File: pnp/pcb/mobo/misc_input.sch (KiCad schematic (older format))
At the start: 9 parts, among them J18 R_LIMIT, J19 P_LIMIT, J20 C_LIMIT, J60 X_LIMIT, J61 Y_LIMIT, J62 Z_LIMIT, J65 ADC_AUX_1, J66 ADC_AUX_2, U6 ‎MPXV5100GC6U

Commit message: took a crack at starting vacuum sensor schematic
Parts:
- removed U6: ‎MPXV5100GC6U, index:‎MPXV5100GC6U, symbol mobo-rescue:‎MPXV5100GC6U-index
- added R? (x8): 10K, symbol Device:R_Small
- added R?: 25K Precision, symbol Device:R_Small
- added U? (x2): 2SMPP-03, symbol index:2SMPP-03
- added U?: INA128, symbol Amplifier_Instrumentation:INA128
- added U? (x6): LM358, symbol Amplifier_Operational:LM358
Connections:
- net labels added: VAC2_SIG
- wire segments 34 -> 75
- no-connect marks 5 -> 4

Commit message: tentative schematic for vacuum, without the right symbol for in-amps
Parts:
- removed U?: 2SMPP-03, symbol index:2SMPP-03
- removed U? (x3): LM358, symbol Amplifier_Operational:LM358
- added R? (x8): 10K, symbol Device:R_Small
- added R?: 25K Precision, symbol Device:R_Small
- added U?: 2SMPP-03, symbol index:2SMPP-03
- added U?: INA128, symbol Amplifier_Instrumentation:INA128
- added U? (x3): LM358, symbol Amplifier_Operational:LM358
- gave numbers to parts that had none: 12
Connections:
- net labels added: +12V
- wire segments 75 -> 118
- no-connect marks 4 -> 6
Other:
- note added: "make this in-amp actually one IC"

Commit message: added reverse polarity protection with a p channel fet
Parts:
- R22, R?: value 10K -> 1K
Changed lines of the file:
@@
 P 6150 2150
 F 0 "R22" H 6000 2200 50  0000 L CNN
-F 1 "10K" H 5800 2100 50  0000 L CNN
+F 1 "1K" H 5800 2100 50  0000 L CNN
 F 2 "" H 6150 2150 50  0001 C CNN
 F 3 "~" H 6150 2150 50  0001 C CNN
@@
 P 6150 4900
 F 0 "R?" H 6000 4950 50  0000 L CNN
-F 1 "10K" H 5800 4850 50  0000 L CNN
+F 1 "1K" H 5800 4850 50  0000 L CNN
 F 2 "" H 6150 4900 50  0001 C CNN
 F 3 "~" H 6150 4900 50  0001 C CNN

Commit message: assigned a footprint to the instrumentation amplifier, deleted all traces from old layout
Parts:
- R19, R20, R21, R22, R23, R24, R25, R26, R27: footprint (none) -> Resistor_SMD:R_0805_2012Metric_Pad1.15x1.40mm_HandSolder
- R28, R29, R30, R31, R32, R33, R34, R35, R36: renamed from R?; footprint (none) -> Resistor_SMD:R_0805_2012Metric_Pad1.15x1.40mm_HandSolder
- U10: footprint (none) -> Package_SO:SOIC-16_3.9x9.9mm_P1.27mm
- gave numbers to parts that had none: 5
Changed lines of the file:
@@
 VAC2_SIG
 $Comp
-L index:2SMPP-03 U?
+L index:2SMPP-03 U12
 U 1 1 5F80C429
 P 4650 2600
-F 0 "U?" H 4650 2577 50  0000 C CNN
+F 0 "U12" H 4650 2577 50  0000 C CNN
 F 1 "2SMPP-03" H 4650 2486 50  0000 C CNN
 F 2 "" H 4650 2600 50  0001 C CNN
@@
 F 0 "U10" H 6600 2300 50  0000 L CNN
 F 1 "INA128" H 6700 2050 50  0000 L CNN
-F 2 "" H 6600 2150 50  0001 C CNN
+F 2 "Package_SO:SOIC-16_3.9x9.9mm_P1.27mm" H 6600 2150 50  0001 C CNN
 F 3 "http://www.ti.com/lit/ds/symlink/ina128.pdf" H 6600 2150 50  0001 C CNN
 	1    6500 2150
@@
 F 0 "R22" H 6000 2200 50  0000 L CNN
 F 1 "1K" H 5800 2100 50  0000 L CNN
-F 2 "" H 6150 2150 50  0001 C CNN
+F 2 "Resistor_SMD:R_0805_2012Metric_Pad1.15x1.40mm_HandSolder" H 6150 2150 50  0001 C CNN
 F 3 "~" H 6150 2150 50  0001 C CNN
 	1    6150 2150
@@
 F 0 "R19" H 3000 1600 50  0000 L CNN
 F 1 "10K" H 2950 1500 50  0000 L CNN
-F 2 "" H 3150 1550 50  0001 C CNN
+F 2 "Resistor_SMD:R_0805_2012Metric_Pad1.15x1.40mm_HandSolder" H 3150 1550 50  0001 C CNN
 F 3 "~" H 3150 1550 50  0001 C CNN
 	1    3150 1550
@@
 F 0 "R20" H 3000 2000 50  0000 L CNN
 F 1 "10K" H 2950 1900 50  0000 L CNN
-F 2 "" H 3150 1950 50  0001 C CNN
+F 2 "Resistor_SMD:R_0805_2012Metric_Pad1.15x1.40mm_HandSolder" H 3150 1950 50  0001 C CNN
 F 3 "~" H 3150 1950 50  0001 C CNN
 	1    3150 1950
@@
 F 0 "R21" V 4000 2450 50  0000 L CNN
 F 1 "25K Precision" V 3800 2050 50  0000 L CNN
-F 2 "" H 3900 2500 50  0001 C CNN
+F 2 "Resistor_SMD:R_0805_2012Metric_Pad1.15x1.40mm_HandSolder" H 3900 2500 50  0001 C CNN
 F 3 "~" H 3900 2500 50  0001 C CNN
 	1    3900 2500
@@
 F 0 "R24" H 7450 1900 50  0000 L CNN
 F 1 "10K" H 7400 1800 50  0000 L CNN
-F 2 "" H 7600 1850 50  0001 C CNN
+F 2 "Resistor_SMD:R_0805_2012Metric_Pad1.15x1.40mm_HandSolder" H 7600 1850 50  0001 C CNN
 F 3 "~" H 7600 1850 50  0001 C CNN
 	1    7600 1850
@@
 F 0 "R25" H 7450 2450 50  0000 L CNN
 F 1 "10K" H 7400 2350 50  0000 L CNN
-F 2 "" H 7600 2400 50  0001 C CNN
+F 2 "Resistor_SMD:R_0805_2012Metric_Pad1.15x1.40mm_HandSolder" H 7600 2400 50  0001 C CNN
 F 3 "~" H 7600 2400 50  0001 C CNN
 	1    7600 2400
@@
 F 0 "R26" H 7800 2450 50  0000 L CNN
 F 1 "10K" H 7750 2350 50  0000 L CNN
-F 2 "" H 7950 2400 50  0001 C CNN
+F 2 "Resistor_SMD:R_0805_2012Metric_Pad1.15x1.40mm_HandSolder" H 7950 2400 50  0001 C CNN
 F 3 "~" H 7950 2400 50  0001 C CNN
 	1    7950 2400
@@
 F 0 "R23" V 7250 2200 50  0000 L CNN
 F 1 "10K" V 7250 2000 50  0000 L CNN
-F 2 "" H 7350 2150 50  0001 C CNN
+F 2 "Resistor_SMD:R_0805_2012Metric_Pad1.15x1.40mm_HandSolder" H 7350 2150 50  0001 C CNN
 F 3 "~" H 7350 2150 50  0001 C CNN
 	1    7350 2150
@@
 F 0 "R27" V 7900 1600 50  0000 L CNN
 F 1 "10K" V 7900 1400 50  0000 L CNN
-F 2 "" H 8000 1550 50  0001 C CNN
+F 2 "Resistor_SMD:R_0805_2012Metric_Pad1.15x1.40mm_HandSolder" H 8000 1550 50  0001 C CNN
 F 3 "~" H 8000 1550 50  0001 C CNN
 	1    8000 1550
@@
 make this in-amp actually one IC
 $Comp
-L index:2SMPP-03 U?
+L index:2SMPP-03 U13
 U 1 1 5F829496
 P 4650 5350
-F 0 "U?" H 4650 5327 50  0000 C CNN
+F 0 "U13" H 4650 5327 50  0000 C CNN
 F 1 "2SMPP-03" H 4650 5236 50  0000 C CNN
 F 2 "" H 4650 5350 50  0001 C CNN
@@
 $EndComp
 $Comp
-L Amplifier_Instrumentation:INA128 U?
+L Amplifier_Instrumentation:INA128 U14
 U 1 1 5F82949C
 P 6500 4900
-F 0 "U?" H 6600 5050 50  0000 L CNN
+F 0 "U14" H 6600 5050 50  0000 L CNN
 F 1 "INA128" H 6700 4800 50  0000 L CNN
 F 2 "" H 6600 4900 50  0001 C CNN
@@
 $EndComp
 $Comp
-L Device:R_Small R?
+L Device:R_Small R31
 U 1 1 5F8294A2
 P 6150 4900
-F 0 "R?" H 6000 4950 50  0000 L CNN
+F 0 "R31" H 6000 4950 50  0000 L CNN
 F 1 "1K" H 5800 4850 50  0000 L CNN
-F 2 "" H 6150 4900 50  0001 C CNN
+F 2 "Resistor_SMD:R_0805_2012Metric_Pad1.15x1.40mm_HandSolder" H 6150 4900 50  0001 C CNN
 F 3 "~" H 6150 4900 50  0001 C CNN
 	1    6150 4900
@@
 	6150 5000 6200 5000
 $Comp
-L power:GND #PWR?
+L power:GND #PWR0190
 U 1 1 5F8294AA
 P 6500 5300
-F 0 "#PWR?" H 6500 5050 50  0001 C CNN
+F 0 "#PWR0190" H 6500 5050 50  0001 C CNN
 F 1 "GND" H 6600 5200 50  0000 C CNN
 F 2 "" H 6500 5300 50  0001 C CNN
@@
 	6500 4600 6500 4500
 $Comp
-L Amplifier_Operational:LM358 U?
+L Amplifier_Operational:LM358 U11
 U 1 1 5F8294B7
 P 3800 4600
-F 0 "U?" H 3800 4967 50  0000 C CNN
+F 0 "U11" H 3800 4967 50  0000 C CNN
 F 1 "LM358" H 3800 4876 50  0000 C CNN
 F 2 "" H 3800 4600 50  0001 C CNN
@@
 $EndComp
 $Comp
-L Amplifier_Operational:LM358 U?
+L Amplifier_Operational:LM358 U6
 U 2 1 5F8294BD
 P 8250 4800
-F 0 "U?" H 8250 5167 50  0000 C CNN
+F 0 "U6" H 8250 5167 50  0000 C CNN
 F 1 "LM358" H 8250 5076 50  0000 C CNN
 F 2 "" H 8250 4800 50  0001 C CNN
@@
 $EndComp
 $Comp
-L Amplifier_Operational:LM358 U?
+L Amplifier_Operational:LM358 U11
 U 3 1 5F8294C3
 P 5750 4050
-F 0 "U?" H 5708 4096 50  0000 L CNN
+F 0 "U11" H 5708 4096 50  0000 L CNN
 F 1 "LM358" H 5708 4005 50  0000 L CNN
 F 2 "" H 5750 4050 50  0001 C CNN
@@
 $EndComp
 $Comp
-L Device:R_Small R?
+L Device:R_Small R28
 U 1 1 5F8294C9
 P 3150 4300
-F 0 "R?" H 3000 4350 50  0000 L CNN
+F 0 "R28" H 3000 4350 50  0000 L CNN
 F 1 "10K" H 2950 4250 50  0000 L CNN
-F 2 "" H 3150 4300 50  0001 C CNN
+F 2 "Resistor_SMD:R_0805_2012Metric_Pad1.15x1.40mm_HandSolder" H 3150 4300 50  0001 C CNN
 F 3 "~" H 3150 4300 50  0001 C CNN
 	1    3150 4300
@@
 $EndComp
 $Comp
-L Device:R_Small R?
+L Device:R_Small R29
 U 1 1 5F8294CF
 P 3150 4700
-F 0 "R?" H 3000 4750 50  0000 L CNN
+F 0 "R29" H 3000 4750 50  0000 L CNN
 F 1 "10K" H 2950 4650 50  0000 L CNN
-F 2 "" H 3150 4700 50  0001 C CNN
+F 2 "Resistor_SMD:R_0805_2012Metric_Pad1.15x1.40mm_HandSolder" H 3150 4700 50  0001 C CNN
 F 3 "~" H 3150 4700 50  0001 C CNN
 	1    3150 4700
@@
 $EndComp
 $Comp
-L power:+5V #PWR?
+L power:+5V #PWR0214
 U 1 1 5F8294D5
 P 3500 3950
-F 0 "#PWR?" H 3500 3800 50  0001 C CNN
+F 0 "#PWR0214" H 3500 3800 50  0001 C CNN
 F 1 "+5V" H 3515 4123 50  0000 C CNN
 F 2 "" H 3500 3950 50  0001 C CNN
@@
 	3150 3950 3500 3950
 $Comp
-L power:GND #PWR?
+L power:GND #PWR0215
 U 1 1 5F8294E1
 P 3500 5250
-F 0 "#PWR?" H 3500 5000 50  0001 C CNN
+F 0 "#PWR0215" H 3500 5000 50  0001 C CNN
 F 1 "GND" H 3600 5150 50  0000 C CNN
 F 2 "" H 3500 5250 50  0001 C CNN
@@
 	5200 4950 5100 4950
 $Comp
-L Device:R_Small R?
+L Device:R_Small R30
 U 1 1 5F8294EC
 P 3900 5250
-F 0 "R?" V 4000 5200 50  0000 L CNN
+F 0 "R30" V 4000 5200 50  0000 L CNN
 F 1 "25K Precision" V 3800 4800 50  0000 L CNN
-F 2 "" H 3900 5250 50  0001 C CNN
+F 2 "Resistor_SMD:R_0805_2012Metric_Pad1.15x1.40mm_HandSolder" H 3900 5250 50  0001 C CNN
 F 3 "~" H 3900 5250 50  0001 C CNN
 	1    3900 5250
@@
 	6500 5250 6500 5300
 $Comp
-L power:GND #PWR?
+L power:GND #PWR0216
 U 1 1 5F8294FF
 P 5650 4350
-F 0 "#PWR?" H 5650 4100 50  0001 C CNN
+F 0 "#PWR0216" H 5650 4100 50  0001 C CNN
 F 1 "GND" H 5750 4250 50  0000 C CNN
 F 2 "" H 5650 4350 50  0001 C CNN
@@
 $EndComp
 $Comp
-L Device:R_Small R?
+L Device:R_Small R33
 U 1 1 5F829505
 P 7600 4600
-F 0 "R?" H 7450 4650 50  0000 L CNN
+F 0 "R33" H 7450 4650 50  0000 L CNN
 F 1 "10K" H 7400 4550 50  0000 L CNN
-F 2 "" H 7600 4600 50  0001 C CNN
+F 2 "Resistor_SMD:R_0805_2012Metric_Pad1.15x1.40mm_HandSolder" H 7600 4600 50  0001 C CNN
 F 3 "~" H 7600 4600 50  0001 C CNN
 	1    7600 4600
@@
 $EndComp
 $Comp
-L Device:R_Small R?
+L Device:R_Small R34
 U 1 1 5F82950B
 P 7600 5150
-F 0 "R?" H 7450 5200 50  0000 L CNN
+F 0 "R34" H 7450 5200 50  0000 L CNN
 F 1 "10K" H 7400 5100 50  0000 L CNN
-F 2 "" H 7600 5150 50  0001 C CNN
+F 2 "Resistor_SMD:R_0805_2012Metric_Pad1.15x1.40mm_HandSolder" H 7600 5150 50  0001 C CNN
 F 3 "~" H 7600 5150 50  0001 C CNN
 	1    7600 5150
@@
 	6500 4500 7600 4500
 $Comp
-L Device:R_Small R?
+L Device:R_Small R35
 U 1 1 5F829518
 P 7950 5150
-F 0 "R?" H 7800 5200 50  0000 L CNN
+F 0 "R35" H 7800 5200 50  0000 L CNN
 F 1 "10K" H 7750 5100 50  0000 L CNN
-F 2 "" H 7950 5150 50  0001 C CNN
+F 2 "Resistor_SMD:R_0805_2012Metric_Pad1.15x1.40mm_HandSolder" H 7950 5150 50  0001 C CNN
 F 3 "~" H 7950 5150 50  0001 C CNN
 	1    7950 5150
@@
 $EndComp
 $Comp
-L Device:R_Small R?
+L Device:R_Small R32
 U 1 1 5F82951E
 P 7350 4900
-F 0 "R?" V 7250 4950 50  0000 L CNN
+F 0 "R32" V 7250 4950 50  0000 L CNN
 F 1 "10K" V 7250 4750 50  0000 L CNN
-F 2 "" H 7350 4900 50  0001 C CNN
+F 2 "Resistor_SMD:R_0805_2012Metric_Pad1.15x1.40mm_HandSolder" H 7350 4900 50  0001 C CNN
 F 3 "~" H 7350 4900 50  0001 C CNN
 	1    7350 4900
@@
 	7800 4900 7950 4900
 $Comp
-L Device:R_Small R?
+L Device:R_Small R36
 U 1 1 5F82952D
 P 8000 4300
-F 0 "R?" V 7900 4350 50  0000 L CNN
+F 0 "R36" V 7900 4350 50  0000 L CNN
 F 1 "10K" V 7900 4150 50  0000 L CNN
-F 2 "" H 8000 4300 50  0001 C CNN
+F 2 "Resistor_SMD:R_0805_2012Metric_Pad1.15x1.40mm_HandSolder" H 8000 4300 50  0001 C CNN
 F 3 "~" H 8000 4300 50  0001 C CNN
 	1    8000 4300
@@
 	4100 5250 4200 5250
 $Comp
-L power:+5V #PWR?
+L power:+5V #PWR0217
 U 1 1 5F82CD91
 P 5650 3750
-F 0 "#PWR?" H 5650 3600 50  0001 C CNN
+F 0 "#PWR0217" H 5650 3600 50  0001 C CNN
 F 1 "+5V" H 5665 3923 50  0000 C CNN
 F 2 "" H 5650 3750 50  0001 C CNN
@@
 $EndComp
 $Comp
-L power:+12V #PWR?
+L power:+12V #PWR0218
 U 1 1 5F8318AD
 P 6500 1750
-F 0 "#PWR?" H 6500 1600 50  0001 C CNN
+F 0 "#PWR0218" H 6500 1600 50  0001 C CNN
 F 1 "+12V" H 6515 1923 50  0000 C CNN
 F 2 "" H 6500 1750 50  0001 C CNN
@@
 Connection ~ 6500 1750
 $Comp
-L power:+12V #PWR?
+L power:+12V #PWR0221
 U 1 1 5F83CC9B
 P 6500 4500
-F 0 "#PWR?" H 6500 4350 50  0001 C CNN
+F 0 "#PWR0221" H 6500 4350 50  0001 C CNN
 F 1 "+12V" H 6515 4673 50  0000 C CNN
 F 2 "" H 6500 4500 50  0001 C CNN

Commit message: added in custom symbols for most parts in vacuum circuit, rewired it with those symbols, redid footprint allocation for the board. ready for layout
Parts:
- removed U10: INA128, Package_SO:SOIC-16_3.9x9.9mm_P1.27mm, symbol Amplifier_Instrumentation:INA128
- removed U11, U6, U9: LM358, symbol Amplifier_Operational:LM358
- removed U13: 2SMPP-03, symbol index:2SMPP-03
- removed U14: INA128, symbol Amplifier_Instrumentation:INA128
- added U10: 2SMPP-03, index:2SMPP-03, symbol index:2SMPP-03
- added U11, U6: LM358, Package_SO:SOP-8_3.9x4.9mm_P1.27mm, symbol index:LM358
- added U13, U9: INA126, Package_SO:SOIC-8-1EP_3.9x4.9mm_P1.27mm_EP2.29x3mm, symbol index:INA126
- R22, R31: value 1K -> 10K
- R26: value 10K -> 25K Precision
- R27, R36: value 10K -> 1K
- R30: value 25K Precision -> 10K
- U12: footprint (none) -> index:2SMPP-03
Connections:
- wire segments 118 -> 150
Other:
- note removed: "Vacuum Sensor"
- note removed: "make this in-amp actually one IC"
- moved on the sheet: R19, R20, R33, U12

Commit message: switched to two 10-pin aux ports
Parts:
- U10, U12: symbol index:2SMPP-03 -> mobo-rescue:2SMPP-03-index
- U11, U6: symbol index:LM358 -> mobo-rescue:LM358-index
- U13, U9: symbol index:INA126 -> mobo-rescue:INA126-index
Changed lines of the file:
@@
 ANALOG1
 $Comp
-L index:2SMPP-03 U12
+L mobo-rescue:2SMPP-03-index U12
 U 1 1 5F80C429
 P 4250 2300
+AR Path="/5F80C429" Ref="U12"  Part="1"
+AR Path="/5EB0C5A0/5F80C429" Ref="U12"  Part="1"
 F 0 "U12" H 4250 2277 50  0000 C CNN
 F 1 "2SMPP-03" H 4250 2186 50  0000 C CNN
@@
 $EndComp
 $Comp
-L index:LM358 U6
+L mobo-rescue:LM358-index U6
 U 1 1 5F927FB6
 P 4250 3100
@@
 $EndComp
 $Comp
-L index:INA126 U9
+L mobo-rescue:INA126-index U9
 U 1 1 5FAC9E96
 P 6400 2200
@@
 VAC2_SIG
 $Comp
-L index:2SMPP-03 U10
+L mobo-rescue:2SMPP-03-index U10
 U 1 1 5FAF3177
 P 7500 4500
+AR Path="/5FAF3177" Ref="U10"  Part="1"
+AR Path="/5EB0C5A0/5FAF3177" Ref="U10"  Part="1"
 F 0 "U10" H 7500 4477 50  0000 C CNN
 F 1 "2SMPP-03" H 7500 4386 50  0000 C CNN
@@
 $EndComp
 $Comp
-L index:LM358 U11
+L mobo-rescue:LM358-index U11
 U 1 1 5FAF3189
 P 7500 5300
@@
 $EndComp
 $Comp
-L index:INA126 U13
+L mobo-rescue:INA126-index U13
 U 1 1 5FAF3206
 P 9650 4400

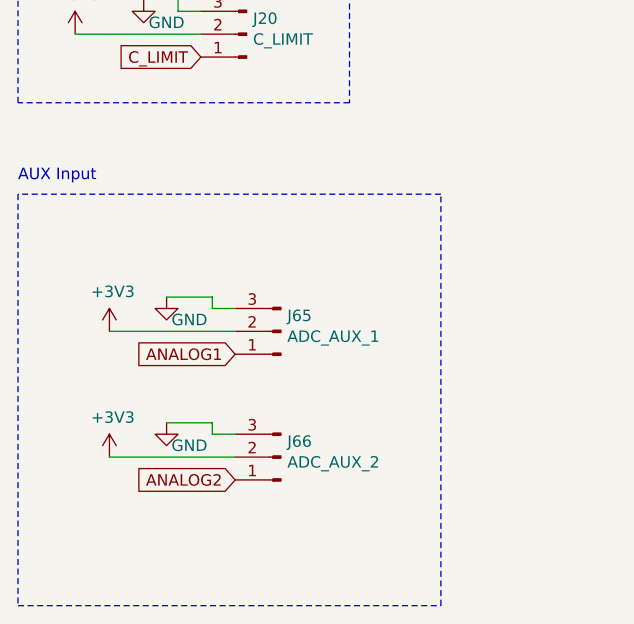
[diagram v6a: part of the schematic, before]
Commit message: added 12v routing to increase current allowed
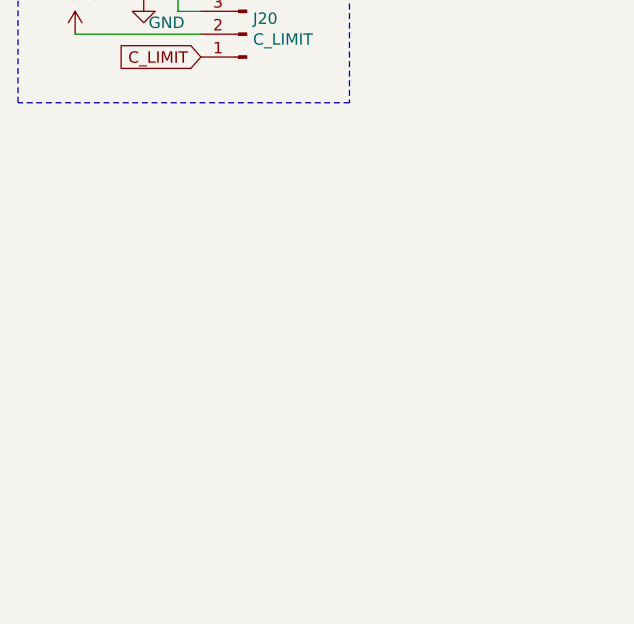
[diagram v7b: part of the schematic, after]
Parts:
- removed J65: ADC_AUX_1, Connector_JST:JST_XH_B3B-XH-A_1x03_P2.50mm_Vertical, symbol Connector:Conn_01x03_Male
- removed J66: ADC_AUX_2, Connector_JST:JST_XH_B3B-XH-A_1x03_P2.50mm_Vertical, symbol Connector:Conn_01x03_Male
- J18, J19, J20, J60, J61, J62: footprint Connector_JST:JST_XH_B3B-XH-A_1x03_P2.50mm_Vertical -> Connector_JST:JST_XH_B03B-XH-A_1x03_P2.50mm_Vertical
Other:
- note removed: "AUX Input"
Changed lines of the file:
@@
 F 0 "J60" H 1722 1182 50  0000 R CNN
 F 1 "X_LIMIT" H 1722 1273 50  0000 R CNN
-F 2 "Connector_JST:JST_XH_B3B-XH-A_1x03_P2.50mm_Vertical" H 1750 1250 50  0001 C CNN
+F 2 "Connector_JST:JST_XH_B03B-XH-A_1x03_P2.50mm_Vertical" H 1750 1250 50  0001 C CNN
 F 3 "~" H 1750 1250 50  0001 C CNN
 	1    1750 1250
@@
 F 0 "J61" H 1722 1732 50  0000 R CNN
 F 1 "Y_LIMIT" H 1722 1823 50  0000 R CNN
-F 2 "Connector_JST:JST_XH_B3B-XH-A_1x03_P2.50mm_Vertical" H 1750 1800 50  0001 C CNN
+F 2 "Connector_JST:JST_XH_B03B-XH-A_1x03_P2.50mm_Vertical" H 1750 1800 50  0001 C CNN
 F 3 "~" H 1750 1800 50  0001 C CNN
 	1    1750 1800
@@
 F 0 "J62" H 1722 2282 50  0000 R CNN
 F 1 "Z_LIMIT" H 1722 2373 50  0000 R CNN
-F 2 "Connector_JST:JST_XH_B3B-XH-A_1x03_P2.50mm_Vertical" H 1750 2350 50  0001 C CNN
+F 2 "Connector_JST:JST_XH_B03B-XH-A_1x03_P2.50mm_Vertical" H 1750 2350 50  0001 C CNN
 F 3 "~" H 1750 2350 50  0001 C CNN
 	1    1750 2350
@@
 Wire Wire Line
 	1450 2250 1450 2200
-$Comp
-L Connector:Conn_01x03_Male J65
-U 1 1 5EF3A019
-P 1900 5350
-F 0 "J65" H 1872 5282 50  0000 R CNN
-F 1 "ADC_AUX_1" H 1872 5373 50  0000 R CNN
-F 2 "Connector_JST:JST_XH_B3B-XH-A_1x03_P2.50mm_Vertical" H 1900 5350 50  0001 C CNN
-F 3 "~" H 1900 5350 50  0001 C CNN
-	1    1900 5350
-	-1   0    0    1
-$EndComp
-$Comp
-L power:GND #PWR0320
-U 1 1 5EF3A025
-P 1400 5200
-F 0 "#PWR0320" H 1400 4950 50  0001 C CNN
-F 1 "GND" H 1500 5100 50  0000 C CNN
-F 2 "" H 1400 5200 50  0001 C CNN
-F 3 "" H 1400 5200 50  0001 C CNN
-	1    1400 5200
-	1    0    0    -1
-$EndComp
-Wire Wire Line
-	1700 5250 1600 5250
-Wire Wire Line
-	1600 5250 1600 5200
-$Comp
-L Connector:Conn_01x03_Male J66
-U 1 1 5EF3A02F
-P 1900 5900
-F 0 "J66" H 1872 5832 50  0000 R CNN
-F 1 "ADC_AUX_2" H 1872 5923 50  0000 R CNN
-F 2 "Connector_JST:JST_XH_B3B-XH-A_1x03_P2.50mm_Vertical" H 1900 5900 50  0001 C CNN
-F 3 "~" H 1900 5900 50  0001 C CNN
-	1    1900 5900
-	-1   0    0    1
-$EndComp
-$Comp
-L power:GND #PWR0322
-U 1 1 5EF3A03B
-P 1400 5750
-F 0 "#PWR0322" H 1400 5500 50  0001 C CNN
-F 1 "GND" H 1500 5650 50  0000 C CNN
-F 2 "" H 1400 5750 50  0001 C CNN
-F 3 "" H 1400 5750 50  0001 C CNN
-	1    1400 5750
-	1    0    0    -1
-$EndComp
-Wire Wire Line
-	1700 5800 1600 5800
-Wire Wire Line
-	1600 5800 1600 5750
 Text GLabel 1550 1350 0    50   Input ~ 0
 X_LIMIT
@@
 Text GLabel 1550 2450 0    50   Input ~ 0
 Z_LIMIT
-Wire Wire Line
-	1400 5200 1600 5200
-Wire Wire Line
-	1150 5350 1700 5350
-Wire Wire Line
-	1400 5750 1600 5750
-Wire Wire Line
-	1150 5900 1700 5900
 Wire Wire Line
 	1300 1100 1450 1100
@@
 F 0 "J18" H 1722 2882 50  0000 R CNN
 F 1 "R_LIMIT" H 1722 2973 50  0000 R CNN
-F 2 "Connector_JST:JST_XH_B3B-XH-A_1x03_P2.50mm_Vertical" H 1750 2950 50  0001 C CNN
+F 2 "Connector_JST:JST_XH_B03B-XH-A_1x03_P2.50mm_Vertical" H 1750 2950 50  0001 C CNN
 F 3 "~" H 1750 2950 50  0001 C CNN
 	1    1750 2950
@@
 F 0 "J19" H 1722 3432 50  0000 R CNN
 F 1 "P_LIMIT" H 1722 3523 50  0000 R CNN
-F 2 "Connector_JST:JST_XH_B3B-XH-A_1x03_P2.50mm_Vertical" H 1750 3500 50  0001 C CNN
+F 2 "Connector_JST:JST_XH_B03B-XH-A_1x03_P2.50mm_Vertical" H 1750 3500 50  0001 C CNN
 F 3 "~" H 1750 3500 50  0001 C CNN
 	1    1750 3500
@@
 F 0 "J20" H 1722 3982 50  0000 R CNN
 F 1 "C_LIMIT" H 1722 4073 50  0000 R CNN
-F 2 "Connector_JST:JST_XH_B3B-XH-A_1x03_P2.50mm_Vertical" H 1750 4050 50  0001 C CNN
+F 2 "Connector_JST:JST_XH_B03B-XH-A_1x03_P2.50mm_Vertical" H 1750 4050 50  0001 C CNN
 F 3 "~" H 1750 4050 50  0001 C CNN
 	1    1750 4050
@@
 Wire Wire Line
 	1000 4050 1550 4050
-$Comp
-L power:+3V3 #PWR0178
-U 1 1 5F17E985
-P 1150 5350
-F 0 "#PWR0178" H 1150 5200 50  0001 C CNN
-F 1 "+3V3" H 1165 5523 50  0000 C CNN
-F 2 "" H 1150 5350 50  0001 C CNN
-F 3 "" H 1150 5350 50  0001 C CNN
-	1    1150 5350
-	1    0    0    -1
-$EndComp
-$Comp
-L power:+3V3 #PWR0179
-U 1 1 5F17F12E
-P 1150 5900
-F 0 "#PWR0179" H 1150 5750 50  0001 C CNN
-F 1 "+3V3" H 1165 6073 50  0000 C CNN
-F 2 "" H 1150 5900 50  0001 C CNN
-F 3 "" H 1150 5900 50  0001 C CNN
-	1    1150 5900
-	1    0    0    -1
-$EndComp
 Wire Notes Line
 	750  850  2200 850
@@
 Text Notes 750  800  0    50   ~ 0
 Limit Switches
-Wire Notes Line
-	750  4750 750  6550
-Wire Notes Line
-	750  6550 2600 6550
-Wire Notes Line
-	2600 6550 2600 4750
-Wire Notes Line
-	2600 4750 750  4750
-Text Notes 750  4700 0    50   ~ 0
-AUX Input
 Text GLabel 4750 3850 2    50   Input ~ 0
 VAC1_SIG
-Text GLabel 1700 6000 0    50   Input ~ 0
-ANALOG2
-Text GLabel 1700 5450 0    50   Input ~ 0
-ANALOG1
 $Comp
 L mobo-rescue:2SMPP-03-index U12
